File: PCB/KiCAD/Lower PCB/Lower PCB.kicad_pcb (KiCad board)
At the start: 2 copper layers, 179.5 x 163.2 mm, 136 parts, among them IC1 ADG608BRZ, IC2 ADG608BRZ, J2 Conn_01x02, M1 Conn_01x02_Pin, M2 Conn_01x02_Pin, M3 Conn_01x02_Pin, M4 Conn_01x02_Pin, Q1 SFH320, Q10 SFH320, Q11 SFH320, Q12 SFH320, Q13 SFH320, Q14 SFH320, Q15 SFH320, Q16 SFH320, Q2 SFH320, Q3 SFH320, Q4 SFH320, Q5 SFH320, Q6 SFH320, Q7 SFH320, Q8 SFH320, Q9 SFH320, U1 ATmega328PB-A, U2 LMD18200, U3 LMD18200, U4 LMD18200, U5 LMD18200, U6 ATmega328PB-A, Y1 Crystal_GND24, Y2 Crystal_GND24

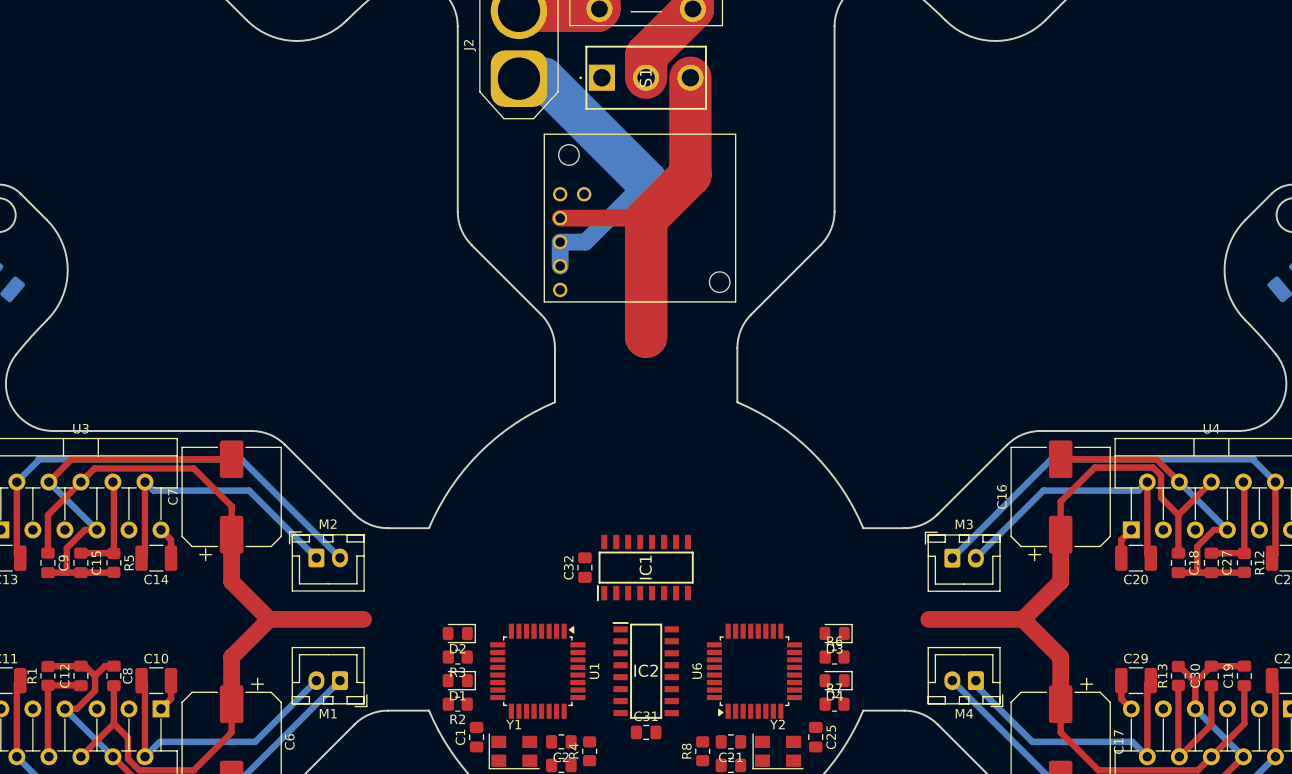
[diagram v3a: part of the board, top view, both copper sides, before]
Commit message: Finished routing main motor controller connections and added connectors
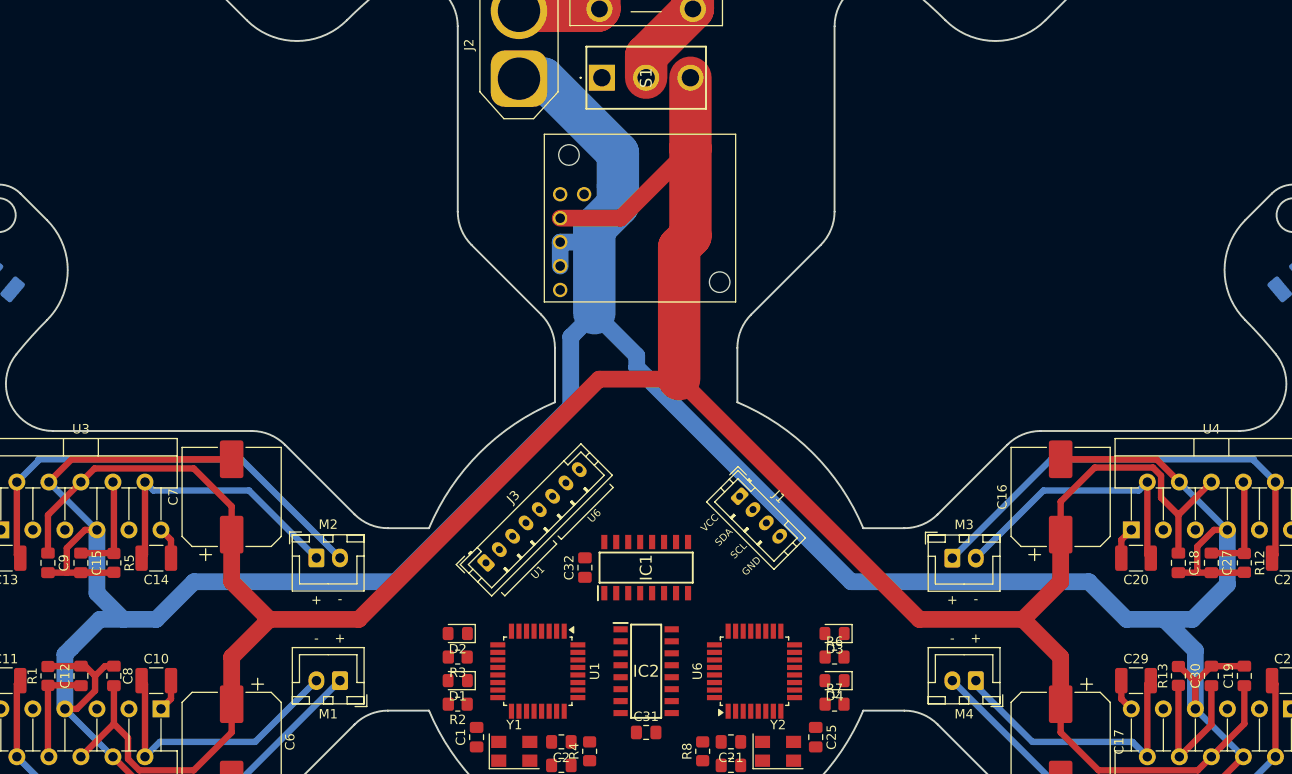
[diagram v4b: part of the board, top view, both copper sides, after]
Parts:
- added J1: Conn_01x04, Connector_JST:JST_PH_B4B-PH-K_1x04_P2.00mm_Vertical, F.Cu at (9.93, -13.1)
- added J3: Conn_01x08, Connector_JST:JST_PH_B8B-PH-K_1x08_P2.00mm_Vertical, F.Cu at (-17.0, -6.00)
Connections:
- net Net-(U1-PB3) renamed MOSI_U1
- net Net-(U1-~{RESET}/PC6) renamed RESET_U1
- net Net-(U6-PB3) renamed MOSI_U6
- net Net-(U6-~{RESET}/PC6) renamed RESET_U6
- C1 pad 2: GND -> MOTOR_1_BRAKE
- C2 pad 1: GND -> MOTOR_1_BRAKE
- C21 pad 1: GND -> MOTOR_1_BRAKE
- C22 pad 1: GND -> MOTOR_1_BRAKE
- C23 pad 1: GND -> MOTOR_1_BRAKE
- C24 pad 1: GND -> MOTOR_1_BRAKE
- C25 pad 2: GND -> MOTOR_1_BRAKE
- C3 pad 1: GND -> MOTOR_1_BRAKE
- C31 pad 2: GND -> MOTOR_1_BRAKE
- C32 pad 2: GND -> MOTOR_1_BRAKE
- C4 pad 1: GND -> MOTOR_1_BRAKE
- C5 pad 1: GND -> MOTOR_1_BRAKE
- D1 pad 1: GND -> MOTOR_1_BRAKE
- D10 pad 1: GND -> MOTOR_1_BRAKE
- D11 pad 1: GND -> MOTOR_1_BRAKE
- D12 pad 1: GND -> MOTOR_1_BRAKE
- D13 pad 1: GND -> MOTOR_1_BRAKE
- D14 pad 1: GND -> MOTOR_1_BRAKE
- D15 pad 1: GND -> MOTOR_1_BRAKE
- D16 pad 1: GND -> MOTOR_1_BRAKE
- D17 pad 1: GND -> MOTOR_1_BRAKE
- D18 pad 1: GND -> MOTOR_1_BRAKE
- D19 pad 1: GND -> MOTOR_1_BRAKE
- D2 pad 1: GND -> MOTOR_1_BRAKE
- D20 pad 1: GND -> MOTOR_1_BRAKE
- D21 pad 1: GND -> MOTOR_1_BRAKE
- D22 pad 1: GND -> MOTOR_1_BRAKE
- D23 pad 1: GND -> MOTOR_1_BRAKE
- D24 pad 1: GND -> MOTOR_1_BRAKE
- D3 pad 1: GND -> MOTOR_1_BRAKE
- D4 pad 1: GND -> MOTOR_1_BRAKE
- D5 pad 1: GND -> MOTOR_1_BRAKE
- D6 pad 1: GND -> MOTOR_1_BRAKE
- D7 pad 1: GND -> MOTOR_1_BRAKE
- D8 pad 1: GND -> MOTOR_1_BRAKE
- D9 pad 1: GND -> MOTOR_1_BRAKE
- IC1 pad 14: GND -> MOTOR_1_BRAKE
- IC1 pad 3: GND -> MOTOR_1_BRAKE
- IC2 pad 14: GND -> MOTOR_1_BRAKE
- IC2 pad 3: GND -> MOTOR_1_BRAKE
- R10 pad 1: GND -> MOTOR_1_BRAKE
- R14 pad 1: GND -> MOTOR_1_BRAKE
- R16 pad 1: GND -> MOTOR_1_BRAKE
- R18 pad 1: GND -> MOTOR_1_BRAKE
- R35 pad 1: GND -> MOTOR_1_BRAKE
- R36 pad 1: GND -> MOTOR_1_BRAKE
- R37 pad 1: GND -> MOTOR_1_BRAKE
- R38 pad 1: GND -> MOTOR_1_BRAKE
- R39 pad 1: GND -> MOTOR_1_BRAKE
- R40 pad 1: GND -> MOTOR_1_BRAKE
- R41 pad 1: GND -> MOTOR_1_BRAKE
- R42 pad 1: GND -> MOTOR_1_BRAKE
- R43 pad 1: GND -> MOTOR_1_BRAKE
- R44 pad 1: GND -> MOTOR_1_BRAKE
- R45 pad 1: GND -> MOTOR_1_BRAKE
- R46 pad 1: GND -> MOTOR_1_BRAKE
- U1 pad 16: unconnected-(U1-PB4-Pad16) -> MISO_U1
- U1 pad 17: unconnected-(U1-PB5-Pad17) -> SCK_U1
- U1 pad 21: GND -> MOTOR_1_BRAKE
- U1 pad 5: GND -> MOTOR_1_BRAKE
- U6 pad 16: unconnected-(U6-PB4-Pad16) -> MISO_U6
- U6 pad 17: unconnected-(U6-PB5-Pad17) -> SCK_U6
- U6 pad 21: GND -> MOTOR_1_BRAKE
- U6 pad 5: GND -> MOTOR_1_BRAKE
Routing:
- net MOTOR_1_BRAKE: track 197.7 -> 379.0 mm
- net +12V: track 221.2 -> 313.1 mm
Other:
- board text added: "+"
- board text added: "-"
- board text added: "GND"
- board text added: "SCL"
- board text added: "SDA"
- board text added: "U1"
- board text added: "U6"
- board text added: "VCC"

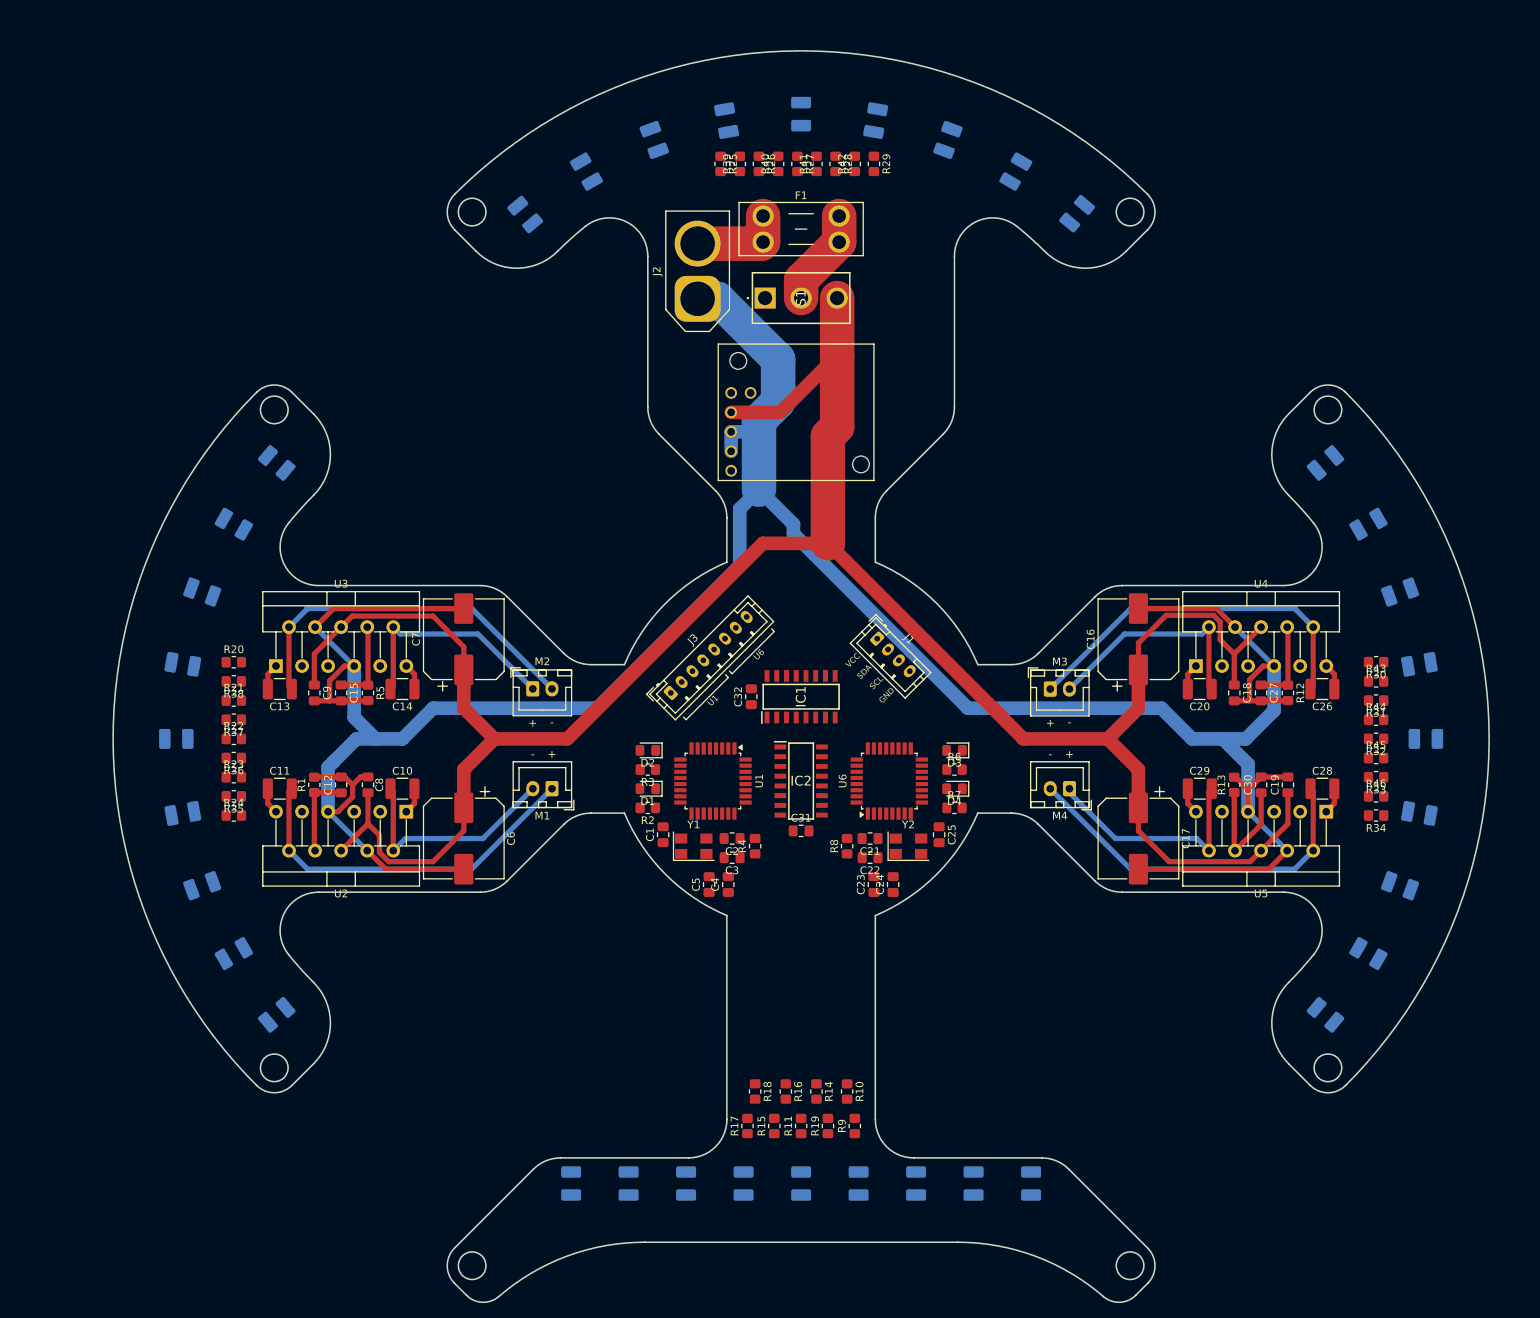
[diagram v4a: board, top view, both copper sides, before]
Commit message: Added labels and fixed label positions
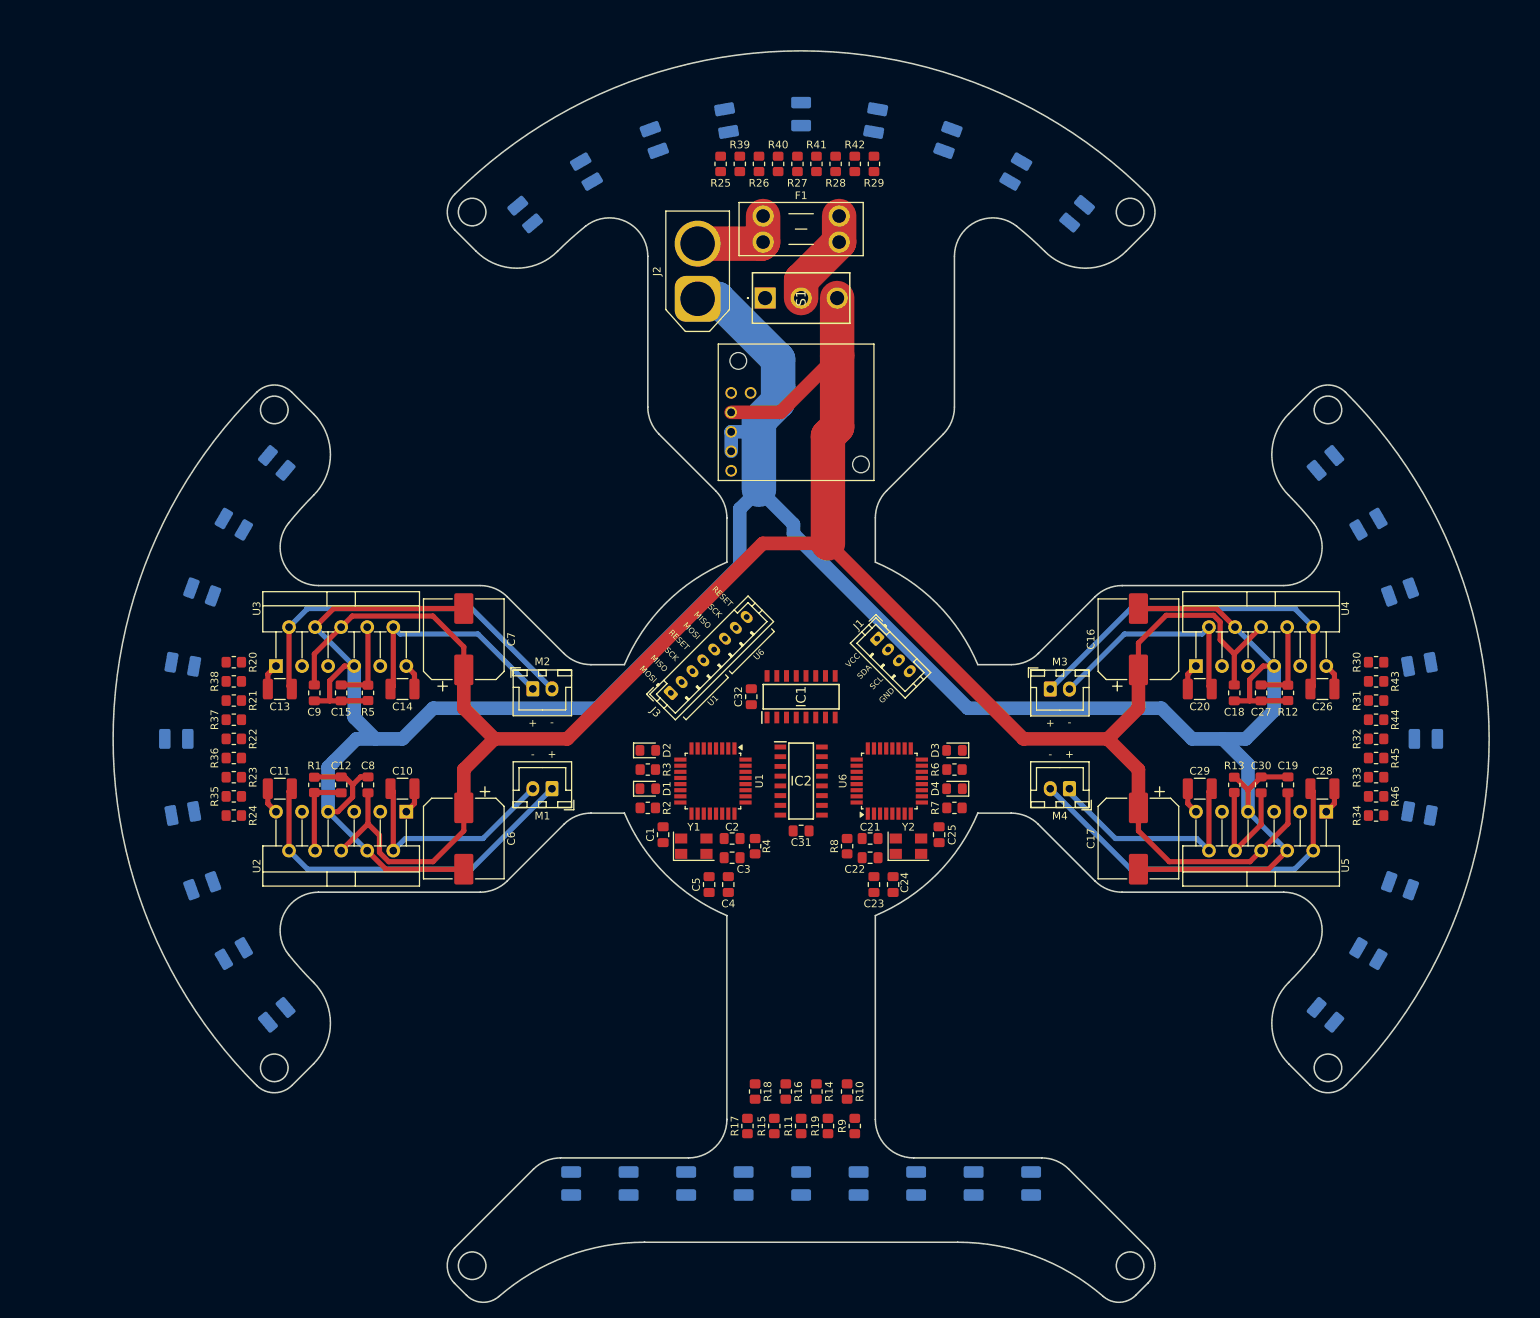
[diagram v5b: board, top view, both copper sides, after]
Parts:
- turned D1 to 0 degrees
- turned D2 to 0 degrees
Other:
- board text added: "MISO"
- board text added: "MOSI"
- board text added: "RESET"
- board text added: "SCK"

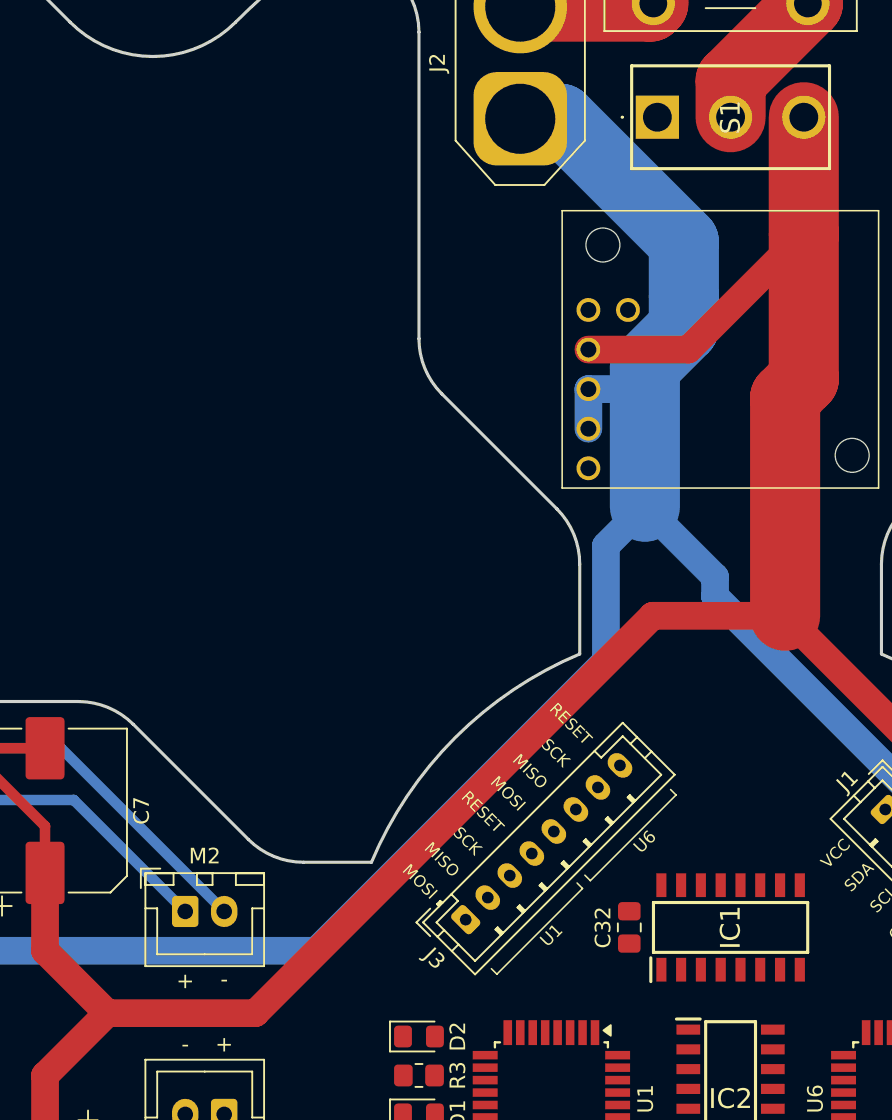
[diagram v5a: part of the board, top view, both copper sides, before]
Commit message: Start to upper PCB
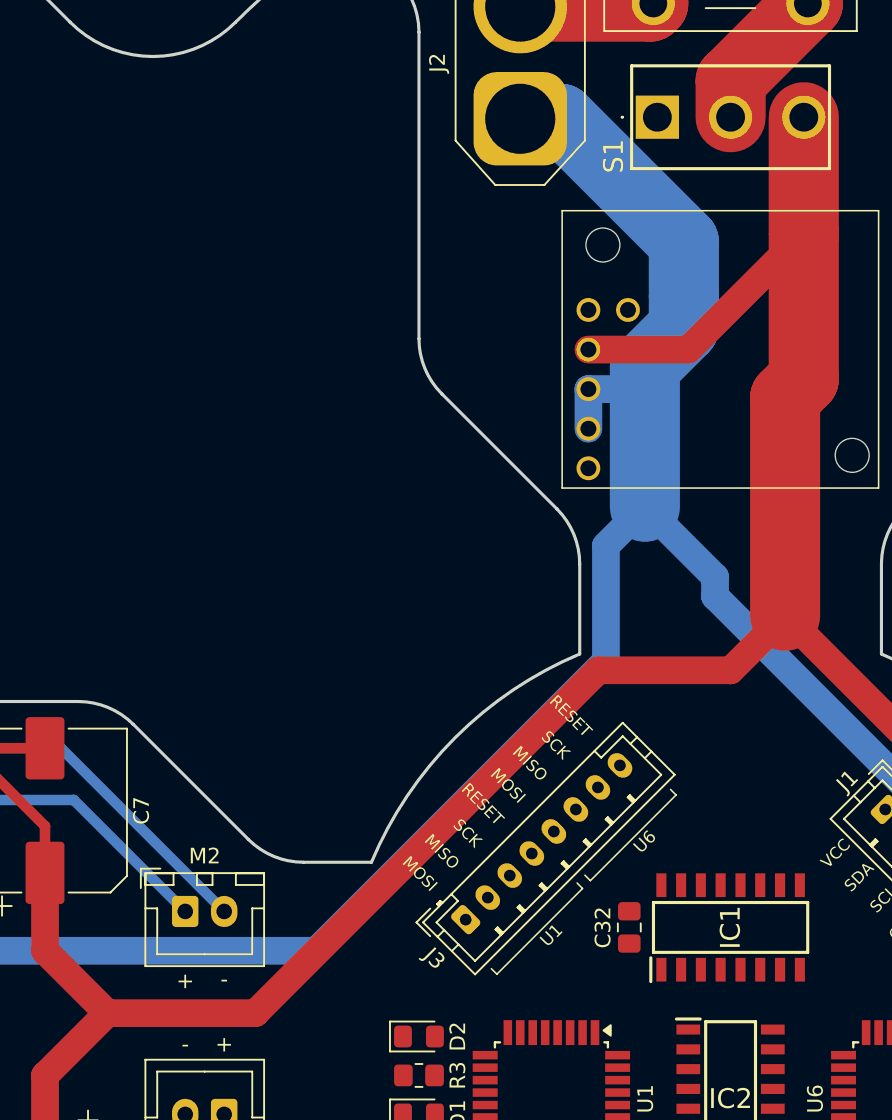
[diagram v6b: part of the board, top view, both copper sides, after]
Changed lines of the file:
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@@
 		(tags "Switch")
 		(property "Reference" "S1"
-			(at 0 -4.7 90)
+			(at 2.5 2.8 90)
 			(layer "F.SilkS")
 			(effects
@@
 	)
 	(gr_text "MOSI"
-		(at -19 -7.5 315)
+		(at -19 -8 315)
 		(layer "F.SilkS")
 		(effects
@@
 	)
 	(gr_text "RESET"
-		(at -14.757359 -11.742641 315)
+		(at -14.757359 -12.242641 315)
 		(layer "F.SilkS")
 		(effects
@@
 	)
 	(gr_text "SCK"
-		(at -16.171573 -10.328427 315)
+		(at -16.171573 -10.828427 315)
 		(layer "F.SilkS")
 		(effects
@@
 	)
 	(gr_text "RESET"
-		(at -9.100505 -17.399495 315)
+		(at -9.100505 -17.899495 315)
 		(layer "F.SilkS")
 		(effects
@@
 	)
 	(gr_text "MISO"
-		(at -11.928932 -14.571068 315)
+		(at -11.928932 -15.071068 315)
 		(layer "F.SilkS")
 		(effects
@@
 	)
 	(gr_text "MOSI"
-		(at -13.343146 -13.156854 315)
+		(at -13.343146 -13.656854 315)
 		(layer "F.SilkS")
 		(effects
@@
 	)
 	(gr_text "SCK"
-		(at -10.514719 -15.985281 315)
+		(at -10.514719 -16.485281 315)
 		(layer "F.SilkS")
 		(effects
@@
 	)
 	(gr_text "MISO"
-		(at -17.585786 -8.914214 315)
+		(at -17.585786 -9.414214 315)
 		(layer "F.SilkS")
 		(effects
@@
 	)
 	(segment
-		(start -5 -25.5)
-		(end -30.5 0)
-		(width 1.78)
-		(layer "F.Cu")
-		(net 28)
-	)
-	(segment
-		(start 3.5 -25.5)
-		(end -5 -25.5)
-		(width 1.78)
-		(layer "F.Cu")
-		(net 28)
-	)
-	(segment
 		(start 40 0)
 		(end 44 -4)
@@
 	)
 	(segment
-		(start 44 9)
-		(end 44 4)
+		(start 0 -22)
+		(end -8.5 -22)
 		(width 1.78)
 		(layer "F.Cu")
@@
 	)
 	(segment
-		(start -40 0)
-		(end -30.5 0)
+		(start 44 9)
+		(end 44 4)
 		(width 1.78)
 		(layer "F.Cu")
@@
 	)
 	(segment
+		(start -30.5 0)
+		(end -40 0)
+		(width 1.78)
+		(layer "F.Cu")
+		(net 28)
+	)
+	(segment
+		(start -8.5 -22)
+		(end -30.5 0)
+		(width 1.78)
+		(layer "F.Cu")
+		(net 28)
+	)
+	(segment
 		(start -48.021 -16.021)
 		(end -44 -12)
@@
 		(layer "F.Cu")
 		(net 28)
+	)
+	(segment
+		(start 3.5 -25.5)
+		(end 0 -22)
+		(width 1.78)
+		(layer "F.Cu")
+		(net 28)
